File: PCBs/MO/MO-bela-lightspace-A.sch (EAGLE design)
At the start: 14 parts

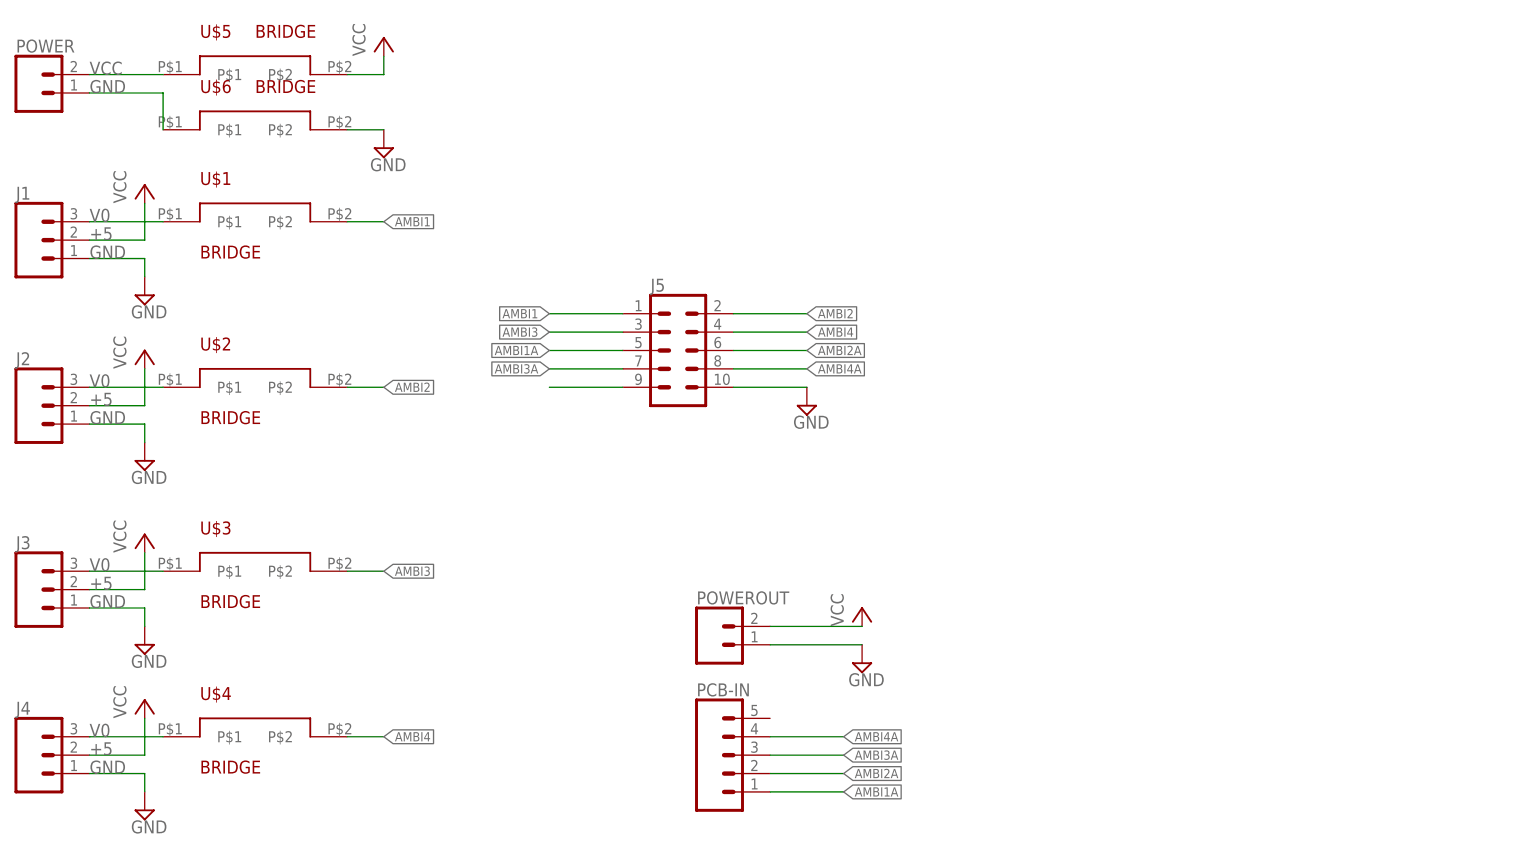
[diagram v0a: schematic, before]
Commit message: lightbox for bela
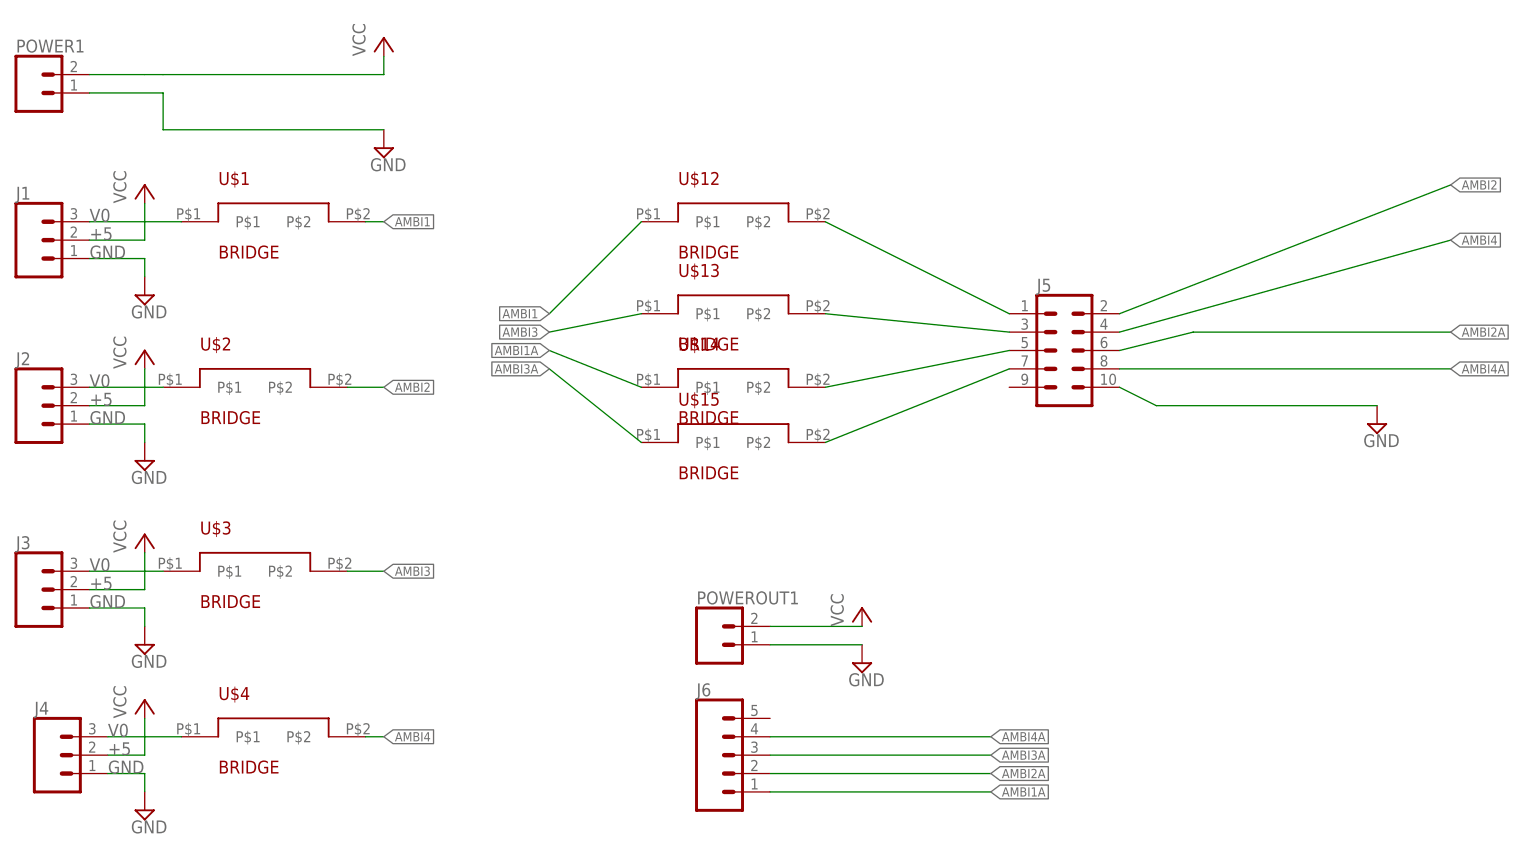
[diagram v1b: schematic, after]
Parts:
- removed POWER: (no value), SparkFun-Connectors:CONN_02POLAR_LOCK
- removed U$5, U$6: BRIDGE, CMU-ArtFab:BRIDGE
- added POWER1: (no value), SparkFun-Connectors:CONN_02LOCK
- added U$12, U$13, U$14, U$15: BRIDGE, CMU-ArtFab:BRIDGE
- renumbered PCB-IN to J6, POWEROUT to POWEROUT1
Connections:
- removed net N$5: J5.9
- removed net N$6: POWER.2, U$5.P$1
- removed net N$7: POWER.1, U$6.P$1
- new net N$10: J5.5, U$14.P$2
- new net N$11: J5.7, U$15.P$2
- new net N$8: J5.1, U$12.P$2
- new net N$9: J5.3, U$13.P$2
- net AMBI1: now also U$12.P$1; no longer J5.1
- net AMBI1A: now also U$14.P$1; no longer J5.5
- net AMBI3: now also U$13.P$1; no longer J5.3
- net AMBI3A: now also U$15.P$1; no longer J5.7
- net GND: now also POWER1.1; no longer U$6.P$2
- net VCC: now also POWER1.2; no longer U$5.P$2
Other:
- moved on the sheet: J4, J5, U$1, U$4
